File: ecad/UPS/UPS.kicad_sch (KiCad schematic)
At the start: 0 parts

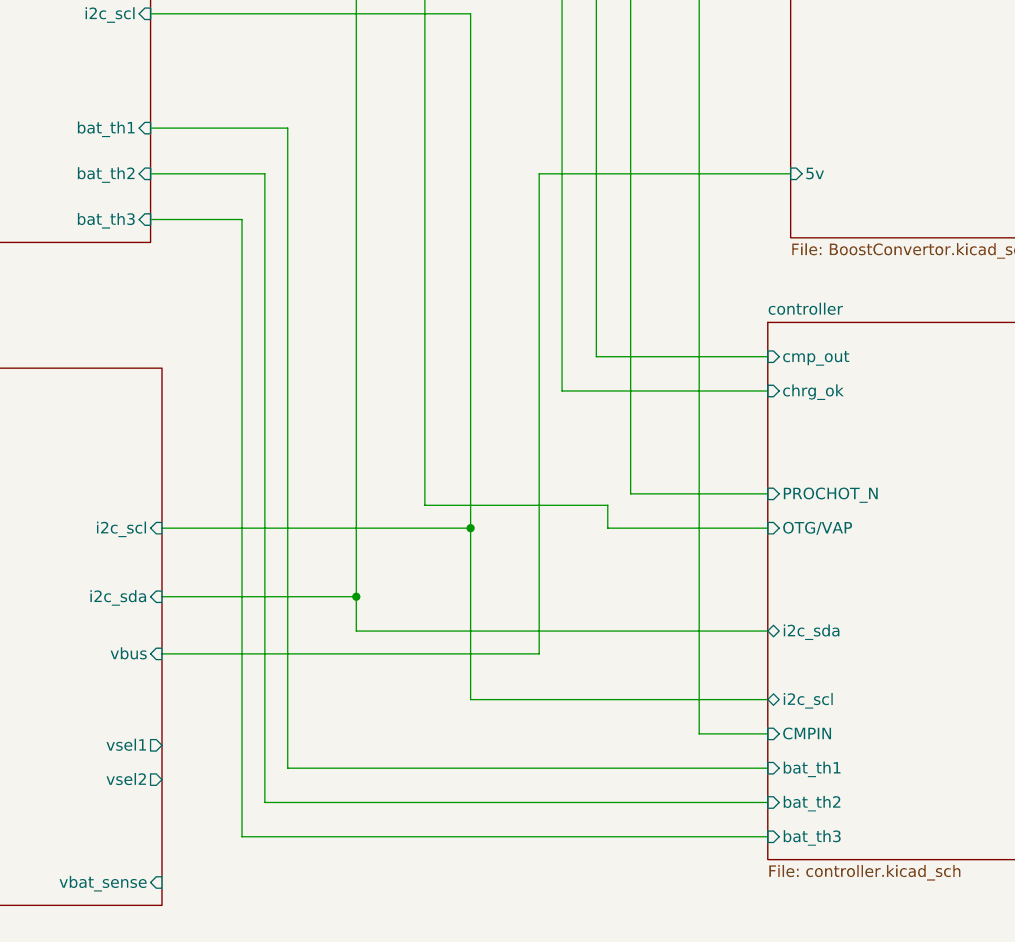
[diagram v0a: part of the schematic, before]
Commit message: Ty's VBATSENSE Changes
Let me know if I messed this part up, did a small amount
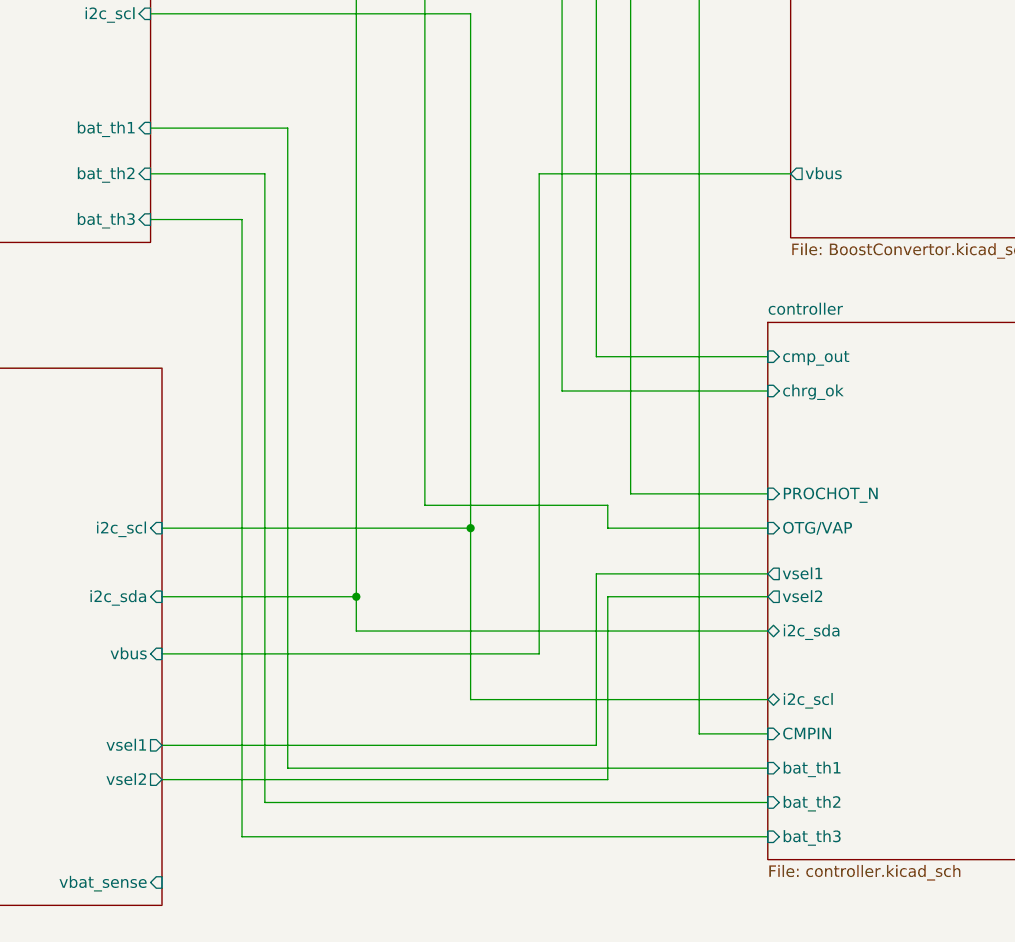
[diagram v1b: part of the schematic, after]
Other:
- sheet BoostConvertor ports: added vbus; removed 5v
- sheet controller ports: added vsel1, vsel2; removed none
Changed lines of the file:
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@@
+	(wire
+		(pts
+			(xy 148.59 143.51) (xy 148.59 124.46)
+		)
+		(stroke
+			(width 0)
+			(type default)
+		)
+	)
+	(wire
+		(pts
+			(xy 149.86 127) (xy 149.86 147.32)
+		)
+		(stroke
+			(width 0)
+			(type default)
+		)
+	)
 	(wire
 		(pts
@@
 	(wire
 		(pts
+			(xy 149.86 147.32) (xy 100.33 147.32)
+		)
+		(stroke
+			(width 0)
+			(type default)
+		)
+	)
+	(wire
+		(pts
 			(xy 121.92 130.81) (xy 121.92 127)
 		)
@@
 	(wire
 		(pts
+			(xy 148.59 124.46) (xy 167.64 124.46)
+		)
+		(stroke
+			(width 0)
+			(type default)
+		)
+	)
+	(wire
+		(pts
 			(xy 100.33 127) (xy 121.92 127)
 		)
@@
 	(wire
 		(pts
+			(xy 100.33 143.51) (xy 148.59 143.51)
+		)
+		(stroke
+			(width 0)
+			(type default)
+		)
+	)
+	(wire
+		(pts
 			(xy 99.06 80.01) (xy 111.76 80.01)
 		)
@@
 		(pts
 			(xy 109.22 85.09) (xy 109.22 153.67)
+		)
+		(stroke
+			(width 0)
+			(type default)
+		)
+	)
+	(wire
+		(pts
+			(xy 167.64 127) (xy 149.86 127)
 		)
 		(stroke
@@
 			)
 		)
+		(pin "vsel2" output
+			(at 167.64 127 180)
+			(effects
+				(font
+					(size 1.27 1.27)
+				)
+				(justify left)
+			)
+		)
+		(pin "vsel1" output
+			(at 167.64 124.46 180)
+			(effects
+				(font
+					(size 1.27 1.27)
+				)
+				(justify left)
+			)
+		)
 		(instances
 			(project "UPS"
@@
 			)
 		)
-		(pin "5v" input
+		(pin "vbus" output
 			(at 170.18 80.01 180)
 			(effects
